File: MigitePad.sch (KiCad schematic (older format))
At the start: 75 parts, among them SW1 SW_Push, U1 ATmega32U4-AU, Y1 16MHz

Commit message: Changed to ProMicro
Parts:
- removed C1, C5, C6: 0.1uF, Capacitor_SMD:C_0805_2012Metric, symbol Device:C_Small
- removed C2, C3: 22pF, Capacitor_SMD:C_0805_2012Metric, symbol Device:C_Small
- removed C4: 1uf, Capacitor_SMD:C_0805_2012Metric, symbol Device:C_Small
- removed C7: 10uF, Capacitor_SMD:C_0805_2012Metric, symbol Device:C_Small
- removed F1: Polyfuse_Small, Fuse:Fuse_1206_3216Metric, symbol Device:Polyfuse_Small
- removed R1, R2: 22, Resistor_SMD:R_0805_2012Metric, symbol Device:R_Small
- removed R3: 10k, Resistor_SMD:R_0805_2012Metric, symbol Device:R_Small
- removed U1: ATmega32U4-AU, Package_QFP:TQFP-44_10x10mm_P0.8mm, symbol MCU_Microchip_ATmega:ATmega32U4-AU
- removed USB1: Molex-0548190589, random-keyboard-parts:Molex-0548190589, symbol random-keyboard-parts:Molex-0548190589
- removed Y1: 16MHz, Crystal:Crystal_SMD_3225-4Pin_3.2x2.5mm_HandSoldering, symbol Device:Crystal_GND24_Small
- added U1: ProMicro, promicro:ProMicro, symbol promicro:ProMicro
- SW1: footprint random-keyboard-parts:SKQG-1155865 -> Keebio-Parts:SW_Tactile_SPST_Angled_MJTP1117
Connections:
- net labels removed: +5V, D+, D-
- wire segments 153 -> 112

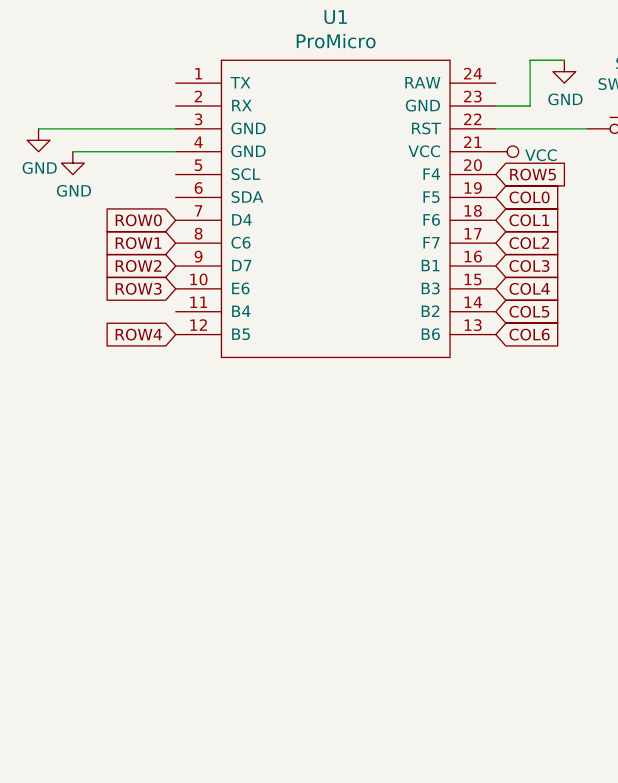
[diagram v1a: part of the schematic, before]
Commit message: Added OLED header
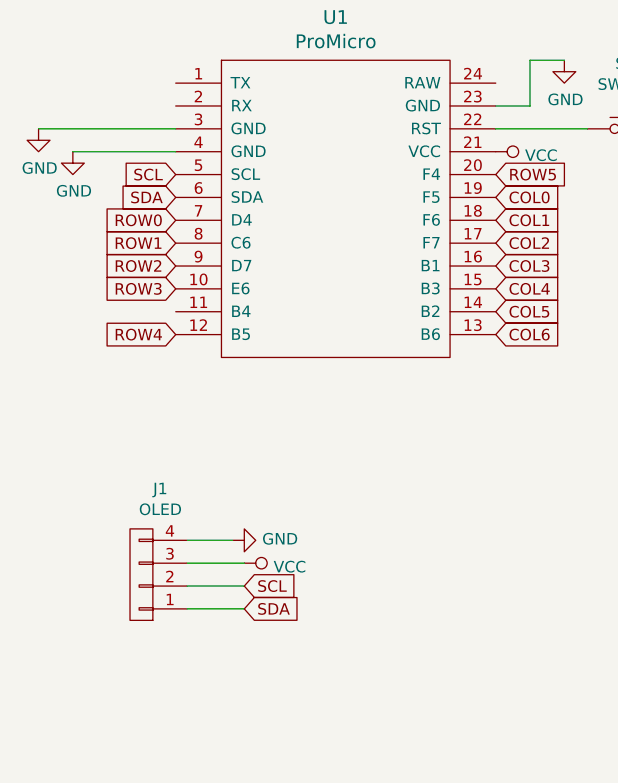
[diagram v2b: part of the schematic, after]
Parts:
- added J1: OLED, Lily58-footprint:MY_SIL-4, symbol oled:OLED
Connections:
- net GND: now also J1.4 (P4)
- net VCC: now also J1.3 (P3)
- net SCL: now reaches U1.5 (SCL)
- net SCL: now also J1.2 (P2)
- net SDA: now reaches U1.6 (SDA)
- net SDA: now also J1.1 (P1)
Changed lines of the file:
@@
 Wire Wire Line
 	1500 1250 1050 1250
+$Comp
+L oled:OLED J1
+U 1 1 5E5D38C4
+P 1350 3100
+F 0 "J1" H 1267 2725 50  0000 C CNN
+F 1 "OLED" H 1267 2816 50  0000 C CNN
+F 2 "Lily58-footprint:MY_SIL-4" H 1350 3100 50  0001 C CNN
+F 3 "" H 1350 3100 50  0000 C CNN
+	1    1350 3100
+	-1   0    0    1
+$EndComp
+$Comp
+L power:GND #PWR0106
+U 1 1 5E5D4A78
+P 1750 2950
+F 0 "#PWR0106" H 1750 2700 50  0001 C CNN
+F 1 "GND" V 1755 2822 50  0000 R CNN
+F 2 "" H 1750 2950 50  0001 C CNN
+F 3 "" H 1750 2950 50  0001 C CNN
+	1    1750 2950
+	0    -1   -1   0
+$EndComp
+Wire Wire Line
+	1550 2950 1750 2950
+Text GLabel 1500 1350 0    50   Input ~ 0
+SCL
+Text GLabel 1500 1450 0    50   Input ~ 0
+SDA
+Text GLabel 1800 3150 2    50   Input ~ 0
+SCL
+Text GLabel 1800 3250 2    50   Input ~ 0
+SDA
+$Comp
+L power:VCC #PWR0107
+U 1 1 5E5DC617
+P 1800 3050
+F 0 "#PWR0107" H 1800 2900 50  0001 C CNN
+F 1 "VCC" V 1817 3178 50  0000 L CNN
+F 2 "" H 1800 3050 50  0001 C CNN
+F 3 "" H 1800 3050 50  0001 C CNN
+	1    1800 3050
+	0    1    1    0
+$EndComp
+Wire Wire Line
+	1550 3050 1800 3050
+Wire Wire Line
+	1550 3150 1800 3150
+Wire Wire Line
+	1550 3250 1800 3250
 $EndSCHEMATC
